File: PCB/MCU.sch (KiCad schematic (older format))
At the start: 41 parts, among them SW1 PTS645VL39-2, SW2 EG1224, U1 ADUM4160, U2 PCA9306, U3 STM32F765VIT6, Y1 TSX-3225 24.0000MF15X-AC3

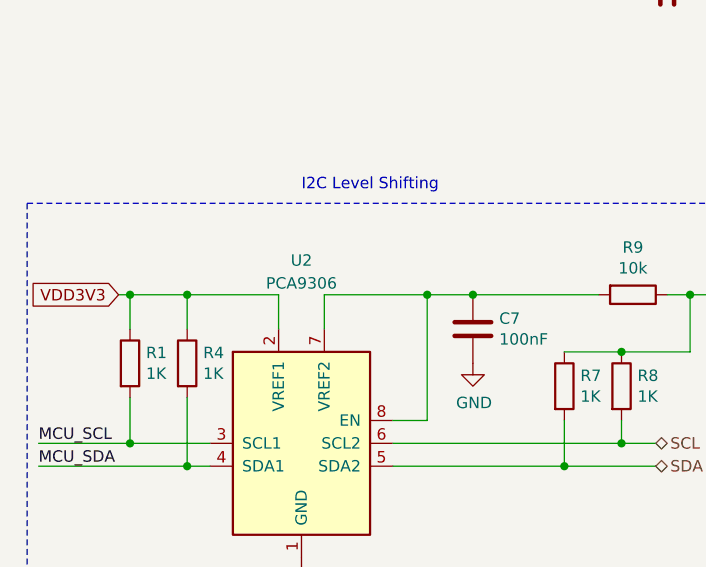
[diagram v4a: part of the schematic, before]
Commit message: Added missing foorprints.
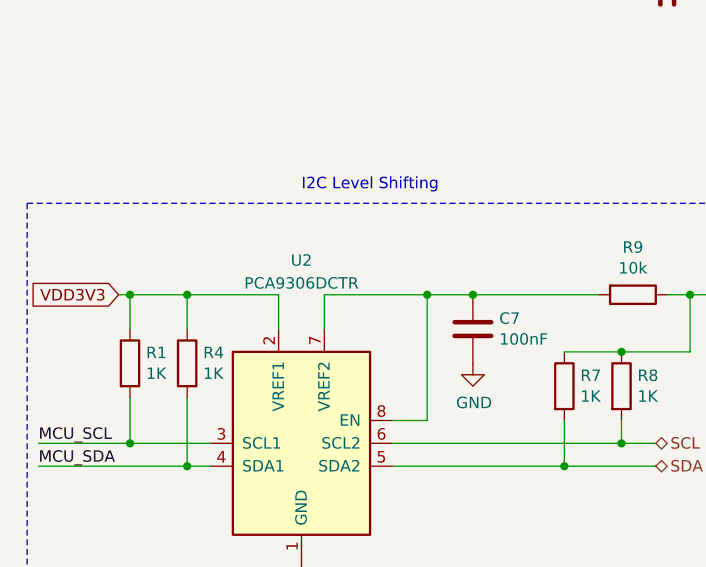
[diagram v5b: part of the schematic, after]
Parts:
- U2: value PCA9306 -> PCA9306DCTR; footprint (none) -> Package_SO:SSOP-8_2.95x2.8mm_P0.65mm
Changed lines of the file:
@@
 P 1750 6000
 F 0 "U2" H 1750 6800 50  0000 C CNN
-F 1 "PCA9306" H 1750 6700 50  0000 C CNN
-F 2 "" H 1350 6350 50  0001 C CNN
+F 1 "PCA9306DCTR" H 1750 6700 50  0000 C CNN
+F 2 "Package_SO:SSOP-8_2.95x2.8mm_P0.65mm" H 1350 6350 50  0001 C CNN
 F 3 "http://www.ti.com/lit/ds/symlink/pca9306.pdf" H 1450 6450 50  0001 C CNN
 	1    1750 6000

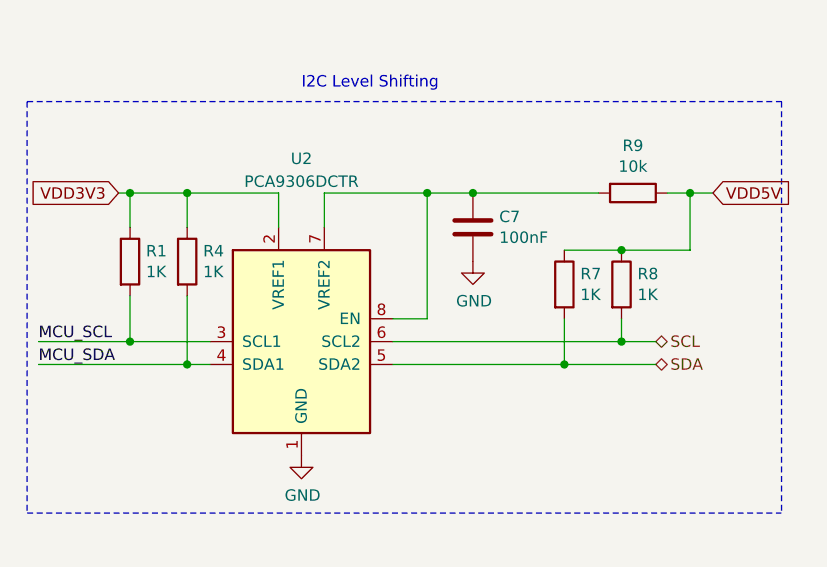
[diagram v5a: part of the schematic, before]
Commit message: Fixed annotations and assignment errors.
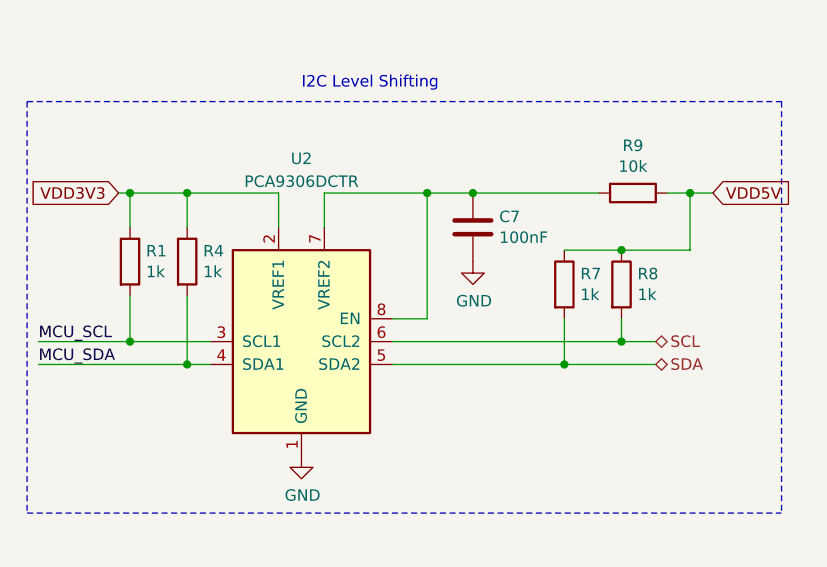
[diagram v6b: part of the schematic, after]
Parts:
- R1, R4, R7, R8: value 1K -> 1k
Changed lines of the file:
@@
 P 1000 5650
 F 0 "R1" H 1070 5696 50  0000 L CNN
-F 1 "1K" H 1070 5605 50  0000 L CNN
+F 1 "1k" H 1070 5605 50  0000 L CNN
 F 2 "Resistor_SMD:R_0603_1608Metric" V 930 5650 50  0001 C CNN
 F 3 "~" H 1000 5650 50  0001 C CNN
@@
 P 1250 5650
 F 0 "R4" H 1320 5696 50  0000 L CNN
-F 1 "1K" H 1320 5605 50  0000 L CNN
+F 1 "1k" H 1320 5605 50  0000 L CNN
 F 2 "Resistor_SMD:R_0603_1608Metric" V 1180 5650 50  0001 C CNN
 F 3 "~" H 1250 5650 50  0001 C CNN
@@
 P 2900 5750
 F 0 "R7" H 2970 5796 50  0000 L CNN
-F 1 "1K" H 2970 5705 50  0000 L CNN
+F 1 "1k" H 2970 5705 50  0000 L CNN
 F 2 "Resistor_SMD:R_0603_1608Metric" V 2830 5750 50  0001 C CNN
 F 3 "~" H 2900 5750 50  0001 C CNN
@@
 P 3150 5750
 F 0 "R8" H 3220 5796 50  0000 L CNN
-F 1 "1K" H 3220 5705 50  0000 L CNN
+F 1 "1k" H 3220 5705 50  0000 L CNN
 F 2 "Resistor_SMD:R_0603_1608Metric" V 3080 5750 50  0001 C CNN
 F 3 "~" H 3150 5750 50  0001 C CNN

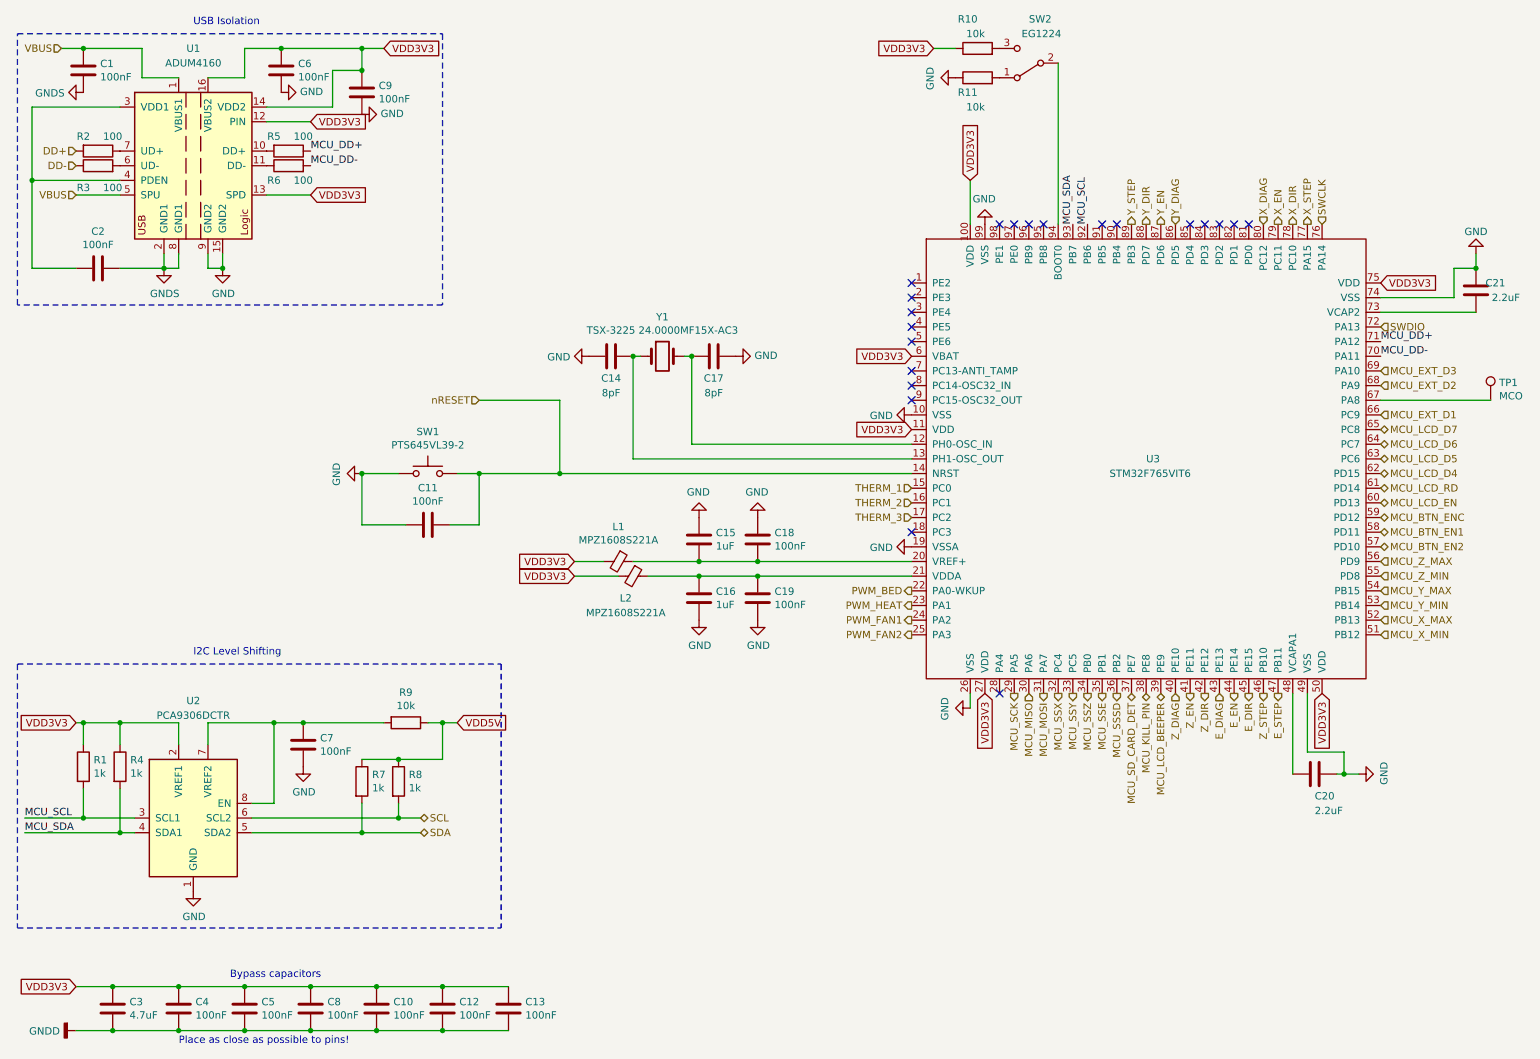
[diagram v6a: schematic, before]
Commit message: Saving work in progress.
Every component now has a 3D mode.
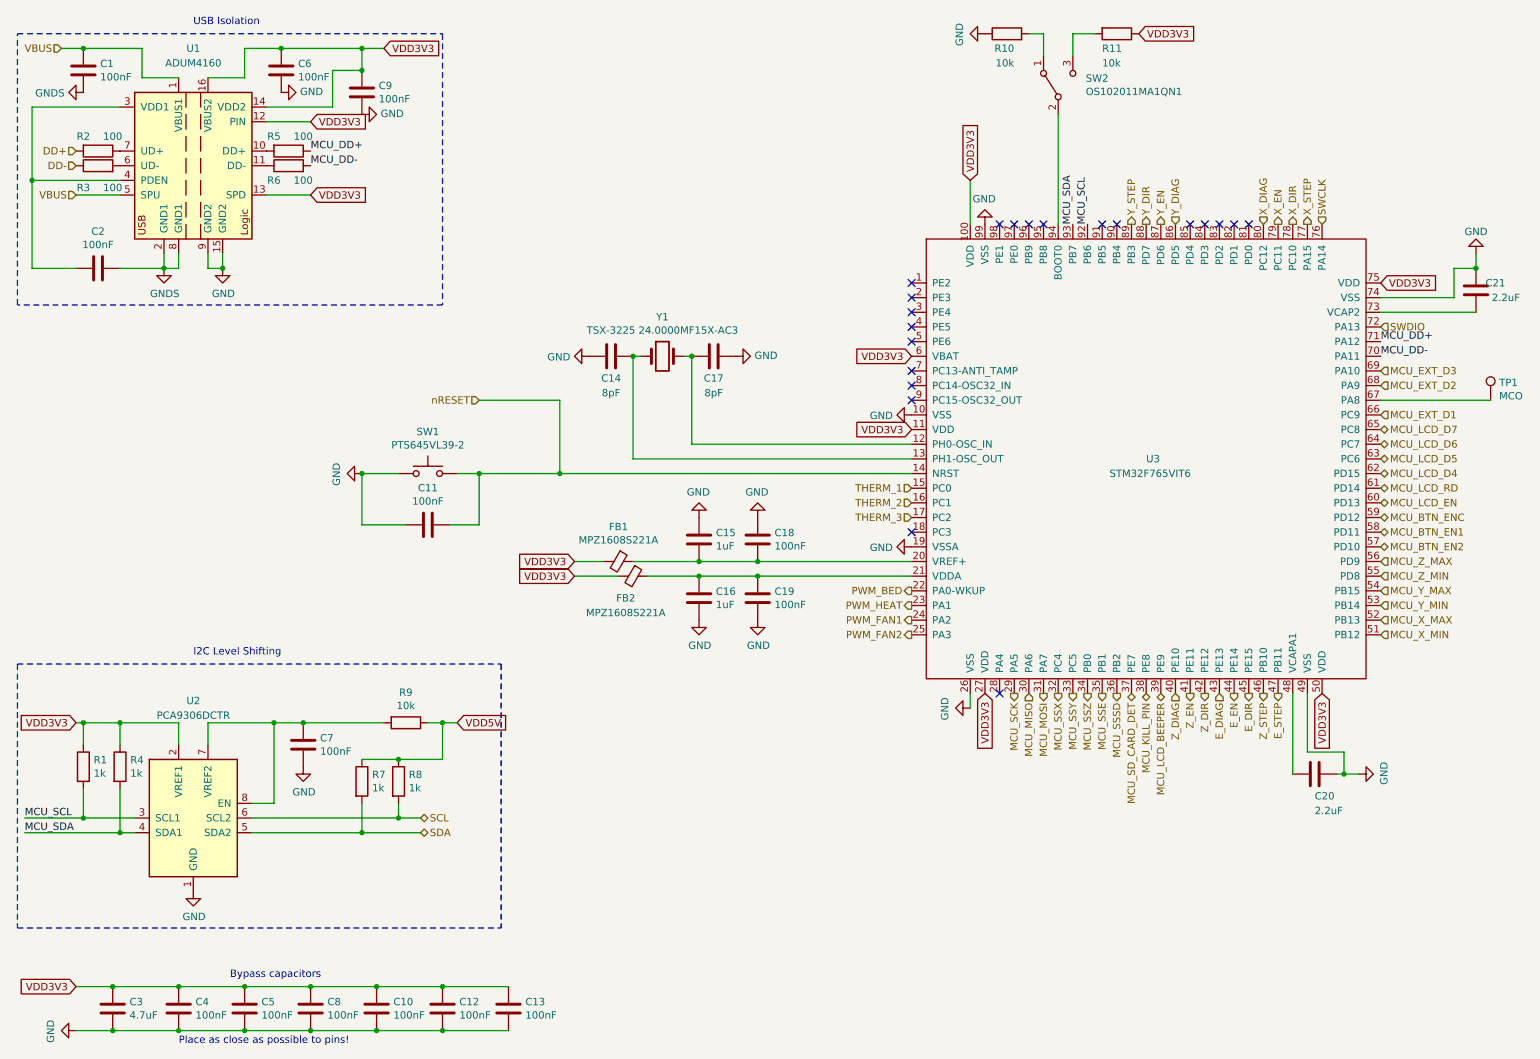
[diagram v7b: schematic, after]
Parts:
- SW2: value EG1224 -> OS102011MA1QN1; footprint Button_Switch_THT:SW_E-Switch_EG1224_SPDT_Angled -> custom-footprints:SW_CuK_OS102011MA1QN1_SPDT_Angled
- U3: footprint Package_QFP:LQFP-100_14x14mm_P0.5mm -> custom-footprints:TQFP-100_14x14mm_P0.5mm
- renumbered L1 to FB1, L2 to FB2, R11 to R10, R10 to R11
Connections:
- net GNDD is gone; now on net GND: C10.2, C12.2, C13.2, C3.2, C4.2, C5.2, C8.2
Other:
- moved on the sheet: R10, R11
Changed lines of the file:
@@
 $EndDescr
 $Comp
-L Switch:SW_SPDT SW2
-U 1 1 5AD0AF5B
-P 7450 850
-F 0 "SW2" H 7450 550 50  0000 R CNN
-F 1 "EG1224" H 7500 650 50  0000 R CNN
-F 2 "Button_Switch_THT:SW_E-Switch_EG1224_SPDT_Angled" H 7450 850 50  0001 C CNN
-F 3 "" H 7450 850 50  0001 C CNN
-	1    7450 850
-	-1   0    0    1
+L Device:R R10
+U 1 1 5AD0B119
+P 7300 650
+F 0 "R10" V 7200 600 50  0000 L CNN
+F 1 "10k" V 7100 600 50  0000 L CNN
+F 2 "Resistor_SMD:R_0603_1608Metric" V 7230 650 50  0001 C CNN
+F 3 "~" H 7300 650 50  0001 C CNN
+	1    7300 650
+	0    -1   -1   0
 $EndComp
 $Comp
 L Device:R R11
-U 1 1 5AD0B119
-P 7100 950
-F 0 "R11" V 7000 950 50  0000 L CNN
-F 1 "10k" V 6900 900 50  0000 L CNN
-F 2 "Resistor_SMD:R_0603_1608Metric" V 7030 950 50  0001 C CNN
-F 3 "~" H 7100 950 50  0001 C CNN
-	1    7100 950
-	0    -1   -1   0
-$EndComp
-$Comp
-L Device:R R10
 U 1 1 5AD0B198
-P 7100 750
-F 0 "R10" V 7300 750 50  0000 L CNN
-F 1 "10k" V 7200 700 50  0000 L CNN
-F 2 "Resistor_SMD:R_0603_1608Metric" V 7030 750 50  0001 C CNN
-F 3 "~" H 7100 750 50  0001 C CNN
-	1    7100 750
-	0    -1   -1   0
-$EndComp
-Wire Wire Line
-	6950 750  6800 750
-Text GLabel 6800 750  0    50   Input ~ 0
+P 8050 650
+F 0 "R11" V 8150 550 50  0000 L CNN
+F 1 "10k" V 8250 550 50  0000 L CNN
+F 2 "Resistor_SMD:R_0603_1608Metric" V 7980 650 50  0001 C CNN
+F 3 "~" H 8050 650 50  0001 C CNN
+	1    8050 650
+	0    1    1    0
+$EndComp
+Text GLabel 8200 650  2    50   Input ~ 0
 VDD3V3
 Text GLabel 6650 2850 0    50   Input ~ 0
@@
 Wire Wire Line
 	3000 7150 3450 7150
-$Comp
-L power:GNDD #PWR01
-U 1 1 5AD0A041
-P 950 7450
-F 0 "#PWR01" H 950 7200 50  0001 C CNN
-F 1 "GNDD" V 954 7340 50  0000 R CNN
-F 2 "" H 950 7450 50  0001 C CNN
-F 3 "" H 950 7450 50  0001 C CNN
-	1    950  7450
-	0    1    1    0
-$EndComp
 Connection ~ 1200 7450
 Wire Wire Line
@@
 $EndComp
 $Comp
-L power:GND #PWR019
+L power:GND #PWR018
 U 1 1 5AF57331
 P 7050 5250
-F 0 "#PWR019" H 7050 5000 50  0001 C CNN
+F 0 "#PWR018" H 7050 5000 50  0001 C CNN
 F 1 "GND" H 7055 5077 50  0000 C CNN
 F 2 "" H 7050 5250 50  0001 C CNN
@@
 	2900 4000 3200 4000
 $Comp
-L power:GND #PWR018
+L power:GND #PWR019
 U 1 1 5AF66D47
-P 6950 950
-F 0 "#PWR018" H 6950 700 50  0001 C CNN
-F 1 "GND" H 6955 777 50  0000 C CNN
-F 2 "" H 6950 950 50  0001 C CNN
-F 3 "" H 6950 950 50  0001 C CNN
-	1    6950 950
+P 7150 650
+F 0 "#PWR019" H 7150 400 50  0001 C CNN
+F 1 "GND" H 7155 477 50  0000 C CNN
+F 2 "" H 7150 650 50  0001 C CNN
+F 3 "" H 7150 650 50  0001 C CNN
+	1    7150 650
 	0    1    1    0
 $EndComp
@@
 	9250 5150 9250 5700
 $Comp
-L Device:Ferrite_Bead_Small L1
+L Device:Ferrite_Bead_Small FB1
 U 1 1 5AF6D789
 P 4650 4250
-F 0 "L1" V 4413 4250 50  0000 C CNN
+F 0 "FB1" V 4413 4250 50  0000 C CNN
 F 1 "MPZ1608S221A" V 4504 4250 50  0000 C CNN
 F 2 "Resistor_SMD:R_0603_1608Metric" V 4580 4250 50  0001 C CNN
@@
 $EndComp
 $Comp
-L Device:Ferrite_Bead_Small L2
+L Device:Ferrite_Bead_Small FB2
 U 1 1 5AF6DF9B
 P 4750 4350
-F 0 "L2" V 4900 4300 50  0000 C CNN
+F 0 "FB2" V 4900 4300 50  0000 C CNN
 F 1 "MPZ1608S221A" V 5000 4300 50  0000 C CNN
 F 2 "Resistor_SMD:R_0603_1608Metric" V 4680 4350 50  0001 C CNN
@@
 F 0 "U3" H 8250 3550 50  0000 L CNN
 F 1 "STM32F765VIT6" H 8000 3450 50  0000 L CNN
-F 2 "Package_QFP:LQFP-100_14x14mm_P0.5mm" H 8250 3550 50  0001 C CNN
+F 2 "custom-footprints:TQFP-100_14x14mm_P0.5mm" H 8250 3550 50  0001 C CNN
 F 3 "http://www.st.com/en/microcontrollers/stm32f765vi.html" H 8250 3550 50  0001 C CNN
 	1    8250 3550
@@
 Connection ~ 5600 4350
 Connection ~ 5600 4250
-Wire Wire Line
-	7650 850  7650 1950
 $Comp
 L Connector_Specialized:Test_Point TP1
@@
 Wire Wire Line
 	5600 4350 6650 4350
+Wire Wire Line
+	7650 1200 7650 1950
+$Comp
+L Switch:SW_SPDT SW2
+U 1 1 5AFBAB59
+P 7650 1000
+F 0 "SW2" V 7696 812 50  0000 R CNN
+F 1 "OS102011MA1QN1" V 7605 812 50  0000 R CNN
+F 2 "custom-footprints:SW_CuK_OS102011MA1QN1_SPDT_Angled" H 7650 1000 50  0001 C CNN
+F 3 "" H 7650 1000 50  0001 C CNN
+	1    7650 1000
+	0    -1   -1   0
+$EndComp
+Wire Wire Line
+	7450 650  7550 650
+Wire Wire Line
+	7550 650  7550 800
+Wire Wire Line
+	7900 650  7750 650
+Wire Wire Line
+	7750 650  7750 800
+$Comp
+L power:GND #PWR0151
+U 1 1 5AFDE2A1
+P 950 7450
+F 0 "#PWR0151" H 950 7200 50  0001 C CNN
+F 1 "GND" H 955 7277 50  0000 C CNN
+F 2 "" H 950 7450 50  0001 C CNN
+F 3 "" H 950 7450 50  0001 C CNN
+	1    950  7450
+	0    1    1    0
+$EndComp
 $EndSCHEMATC

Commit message: Removed logic level converter. Changed LDO.
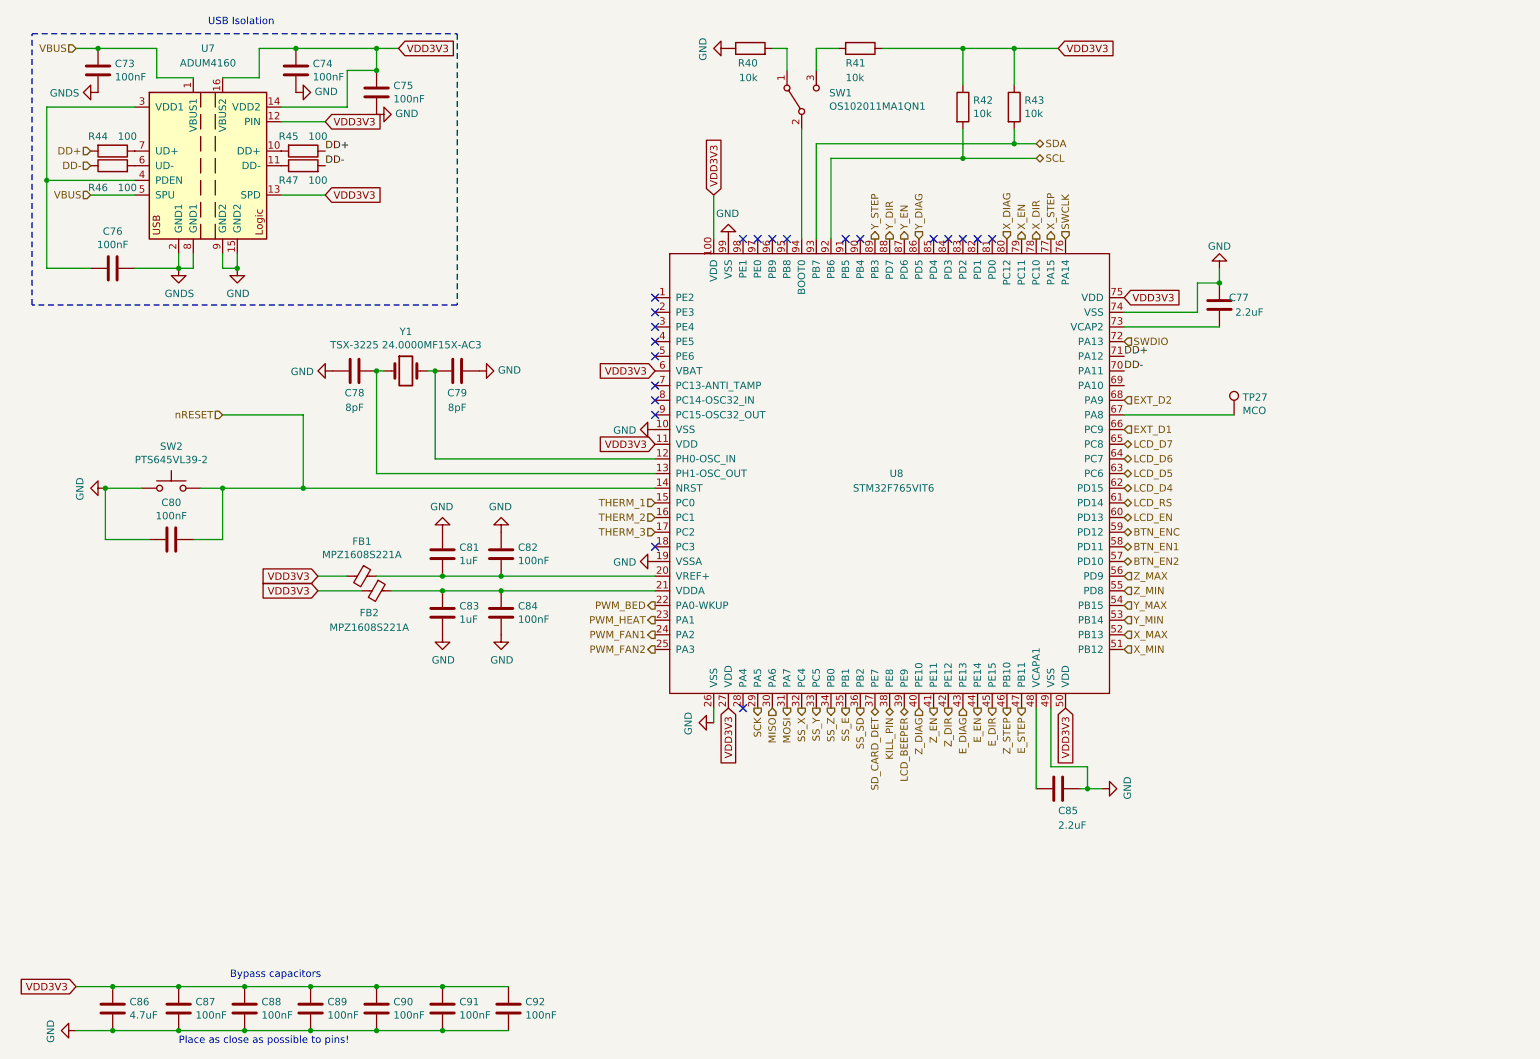
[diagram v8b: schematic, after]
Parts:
- removed C7: 100nF, Capacitor_SMD:C_0603_1608Metric, symbol Device:C
- removed R1, R4: 1k, Resistor_SMD:R_0603_1608Metric, symbol Device:R
- removed R9: 10k, Resistor_SMD:R_0603_1608Metric, symbol Device:R
- removed U2: PCA9306DCTR, Package_SO:SSOP-8_2.95x2.8mm_P0.65mm, symbol Interface:PCA9306
- R42: renamed from R7; value 1k -> 10k
- R43: renamed from R8; value 1k -> 10k
- renumbered C1 to C73, C6 to C74, C9 to C75, C2 to C76, C21 to C77, C14 to C78, C17 to C79, C11 to C80, C15 to C81, C18 to C82, C16 to C83, C19 to C84, C20 to C85, C3 to C86, C4 to C87, C5 to C88, C8 to C89, C10 to C90, C12 to C91, C13 to C92, R10 to R40, R11 to R41, R2 to R44, R5 to R45, R3 to R46, R6 to R47, SW2 to SW1, SW1 to SW2, TP1 to TP27, U1 to U7, U3 to U8
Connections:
- net MCU_DD+ is gone; now on net DD+: R45.1, U8.71 (PA12)
- net MCU_DD- is gone; now on net DD-: R47.2, U8.70 (PA11)
- net MCU_SCL is gone; now on net SCL: U8.92 (PB6)
- net MCU_SDA is gone; now on net SDA: U8.93 (PB7)
- net VDD5V is gone; now on net VDD3V3: R42.1, R43.1
- net SCL: now also R42.2; no longer R43.2
- net SDA: now also R43.2; no longer R42.2
- net MCU_BTN_EN1 renamed BTN_EN1
- net MCU_BTN_EN2 renamed BTN_EN2
- net MCU_BTN_ENC renamed BTN_ENC
- net MCU_EXT_D1 renamed EXT_D1
- net MCU_EXT_D2 renamed EXT_D2
- net MCU_EXT_D3: no longer names the net of U8.69 (PA10)
- net MCU_KILL_PIN renamed KILL_PIN
- net MCU_LCD_BEEPER renamed LCD_BEEPER
- net MCU_LCD_D4 renamed LCD_D4
- net MCU_LCD_D5 renamed LCD_D5
- net MCU_LCD_D6 renamed LCD_D6
- net MCU_LCD_D7 renamed LCD_D7
- net MCU_LCD_EN renamed LCD_EN
- net MCU_LCD_RD renamed LCD_RS
- net MCU_MISO renamed MISO
- net MCU_MOSI renamed MOSI
- net MCU_SCK renamed SCK
- net MCU_SD_CARD_DET renamed SD_CARD_DET
- net MCU_SSE renamed SS_E
- net MCU_SSSD renamed SS_SD
- net MCU_SSX renamed SS_X
- net MCU_SSY renamed SS_Y
- net MCU_SSZ renamed SS_Z
- net MCU_X_MAX renamed X_MAX
- net MCU_X_MIN renamed X_MIN
- net MCU_Y_MAX renamed Y_MAX
- net MCU_Y_MIN renamed Y_MIN
- net MCU_Z_MAX renamed Z_MAX
- net MCU_Z_MIN renamed Z_MIN
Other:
- note removed: "I2C Level Shifting"
- moved on the sheet: C73, C74, C75, C76, C77, C78, C79, C80, C81, C82, C83, C84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
